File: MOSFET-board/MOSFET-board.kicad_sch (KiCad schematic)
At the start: 5 parts, among them J2 DB15_Female, J3 DB15_Female, J4 Bus_PCI_Express_x16, U11 PCF8575_Breakout

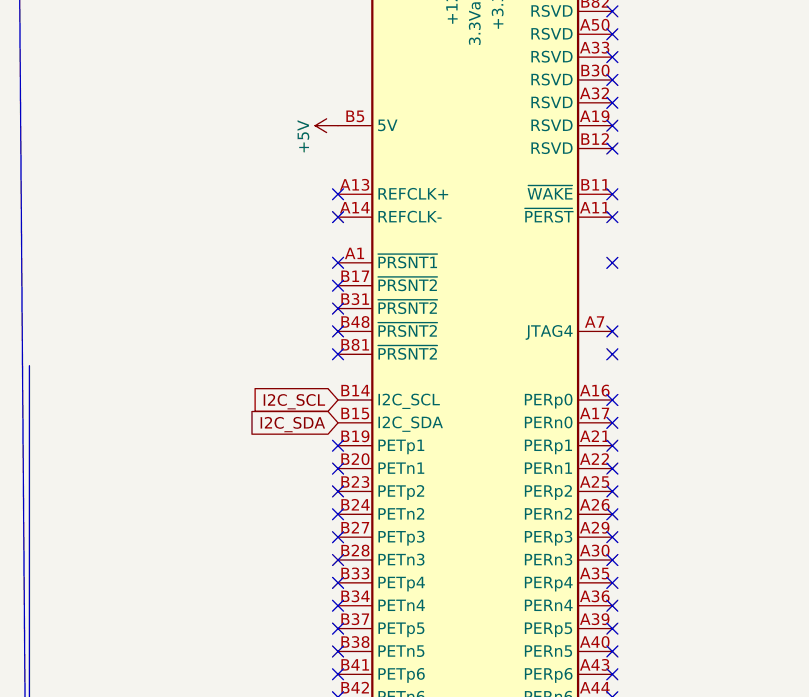
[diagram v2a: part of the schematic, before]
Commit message: mosfet board updates. GND tracing removals and aux scl/sda
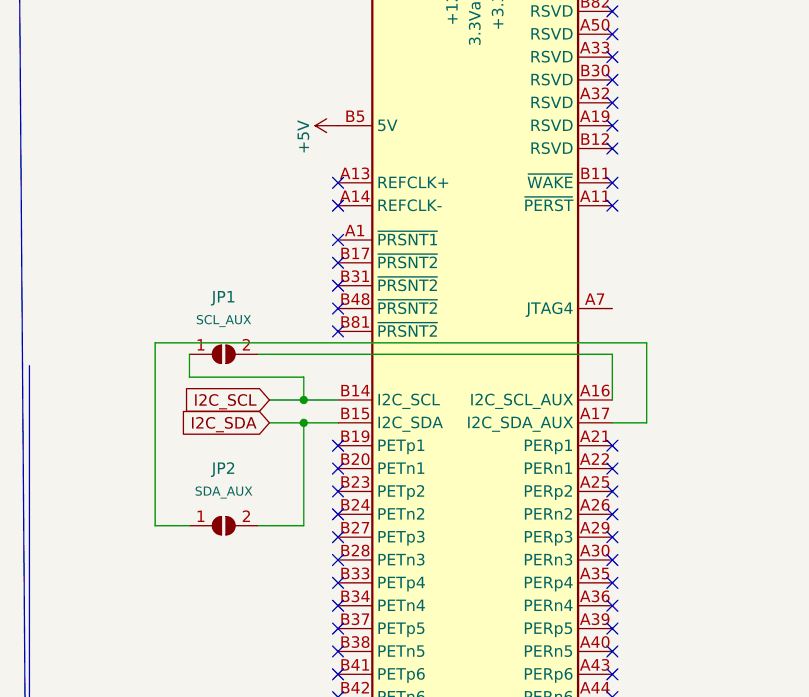
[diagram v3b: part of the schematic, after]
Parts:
- added JP1: SCL_AUX, Jumper:SolderJumper-2_P1.3mm_Open_Pad1.0x1.5mm, symbol Jumper:SolderJumper_2_Open
- added JP2: SDA_AUX, Jumper:SolderJumper-2_P1.3mm_Open_Pad1.0x1.5mm, symbol Jumper:SolderJumper_2_Open
- J4: footprint Connector_PCBEdge:BUS_PCIexpress_x16 -> PCIe_x16_DAQ:Custom-16x-PCIELock
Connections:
- net I2C_SCL: now also JP1.1 (A)
- net I2C_SDA: now also JP2.2 (B)
- net at J4.A16 (I2C_SCL_AUX): now also JP1.2 (B)
- net at J4.A17 (I2C_SDA_AUX): now also JP2.1 (A)
- no-connect marks 98 -> 93
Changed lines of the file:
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@@
   (junction (at 63.5 250.19) (diameter 0) (color 0 0 0 0)
   )
+  (junction (at 43.18 82.55) (diameter 0) (color 0 0 0 0)
+  )
   (junction (at 21.59 255.524) (diameter 0) (color 0 0 0 0)
   )
@@
   )
   (junction (at 21.59 250.444) (diameter 0) (color 0 0 0 0)
+  )
+  (junction (at 43.18 85.09) (diameter 0) (color 0 0 0 0)
   )
   (no_connect (at 77.47 115.57))
@@
   (no_connect (at 77.47 135.89))
   (no_connect (at 74.93 275.59))
-  (no_connect (at 46.99 62.23))
+  (no_connect (at 46.99 60.96))
   (no_connect (at 46.99 97.79))
   (no_connect (at 77.47 161.29))
@@
   (no_connect (at 77.47 113.03))
   (no_connect (at 29.21 208.28))
-  (no_connect (at 46.99 77.47))
+  (no_connect (at 46.99 64.77))
   (no_connect (at 46.99 95.25))
   (no_connect (at 77.47 105.41))
@@
   (no_connect (at 77.47 133.35))
   (no_connect (at 77.47 128.27))
-  (no_connect (at 77.47 62.23))
+  (no_connect (at 77.47 60.96))
   (no_connect (at 46.99 148.59))
-  (no_connect (at 77.47 85.09))
   (no_connect (at 46.99 113.03))
   (no_connect (at 77.47 146.05))
@@
   (no_connect (at 46.99 74.93))
   (no_connect (at 74.93 273.05))
-  (no_connect (at 77.47 82.55))
   (no_connect (at 33.02 273.304))
   (no_connect (at 57.15 205.74))
@@
   (no_connect (at 77.47 156.21))
   (no_connect (at 33.02 270.764))
-  (no_connect (at 77.47 67.31))
   (no_connect (at 33.02 268.224))
   (no_connect (at 46.99 151.13))
@@
   (no_connect (at 77.47 110.49))
   (no_connect (at 46.99 125.73))
-  (no_connect (at 77.47 74.93))
   (no_connect (at 77.47 44.45))
   (no_connect (at 57.15 208.28))
   (no_connect (at 77.47 95.25))
   (no_connect (at 77.47 123.19))
-  (no_connect (at 46.99 59.69))
-  (no_connect (at 77.47 77.47))
+  (no_connect (at 46.99 58.42))
   (no_connect (at 29.21 203.2))
   (no_connect (at 46.99 133.35))
@@
   (no_connect (at 77.47 125.73))
   (no_connect (at 77.47 49.53))
-  (no_connect (at 77.47 59.69))
+  (no_connect (at 77.47 58.42))
   (wire (pts (xy 33.02 245.364) (xy 21.59 245.364))
     (stroke (width 0) (type default))
@@
     (stroke (width 0) (type default))
   )
+  (wire (pts (xy 26.67 76.2) (xy 26.67 96.52))
+    (stroke (width 0) (type default))
+  )
   (wire (pts (xy 222.758 143.002) (xy 222.758 144.272))
     (stroke (width 0) (type default))
@@
     (stroke (width 0) (type default))
   )
+  (wire (pts (xy 77.47 85.09) (xy 81.28 85.09))
+    (stroke (width 0) (type default))
+  )
   (wire (pts (xy 62.23 30.48) (xy 64.77 30.48))
     (stroke (width 0) (type default))
   )
+  (wire (pts (xy 38.1 96.52) (xy 43.18 96.52))
+    (stroke (width 0) (type default))
+  )
+  (wire (pts (xy 81.28 85.09) (xy 81.28 76.2))
+    (stroke (width 0) (type default))
+  )
   (polyline (pts (xy 11.684 216.662) (xy 11.938 279.4))
     (stroke (width 0) (type default))
@@
     (stroke (width 0) (type default))
   )
+  (wire (pts (xy 43.18 96.52) (xy 43.18 85.09))
+    (stroke (width 0) (type default))
+  )
   (wire (pts (xy 63.5 255.27) (xy 74.93 255.27))
     (stroke (width 0) (type default))
@@
     (stroke (width 0) (type default))
   )
+  (wire (pts (xy 26.67 96.52) (xy 30.48 96.52))
+    (stroke (width 0) (type default))
+  )
   (wire (pts (xy 21.59 260.604) (xy 21.59 265.684))
     (stroke (width 0) (type default))
@@
     (stroke (width 0) (type default))
   )
+  (wire (pts (xy 43.18 82.55) (xy 46.99 82.55))
+    (stroke (width 0) (type default))
+  )
   (wire (pts (xy 203.454 144.272) (xy 203.454 143.002))
     (stroke (width 0) (type default))
@@
     (stroke (width 0) (type default))
   )
+  (wire (pts (xy 81.28 76.2) (xy 26.67 76.2))
+    (stroke (width 0) (type default))
+  )
   (wire (pts (xy 52.07 20.32) (xy 54.61 20.32))
     (stroke (width 0) (type default))
@@
     (stroke (width 0) (type default))
   )
+  (wire (pts (xy 43.18 85.09) (xy 46.99 85.09))
+    (stroke (width 0) (type default))
+  )
   (wire (pts (xy 64.77 29.21) (xy 64.77 30.48))
     (stroke (width 0) (type default))
@@
     (stroke (width 0) (type default))
   )
+  (wire (pts (xy 39.37 82.55) (xy 43.18 82.55))
+    (stroke (width 0) (type default))
+  )
   (polyline (pts (xy 118.11 154.94) (xy 233.68 154.94))
     (stroke (width 0) (type default))
@@
     (stroke (width 0) (type default))
   )
+  (wire (pts (xy 30.48 77.47) (xy 30.48 80.01))
+    (stroke (width 0) (type default))
+  )
   (polyline (pts (xy 12.7 12.7) (xy 233.68 12.7))
     (stroke (width 0) (type default))
@@
     (stroke (width 0) (type default))
   )
+  (wire (pts (xy 77.47 77.47) (xy 38.1 77.47))
+    (stroke (width 0) (type default))
+  )
+  (wire (pts (xy 30.48 80.01) (xy 43.18 80.01))
+    (stroke (width 0) (type default))
+  )
   (polyline (pts (xy 118.11 147.32) (xy 142.24 147.32))
     (stroke (width 0) (type default))
@@
     (stroke (width 0) (type default))
   )
+  (wire (pts (xy 77.47 82.55) (xy 77.47 77.47))
+    (stroke (width 0) (type default))
+  )
   (wire (pts (xy 62.23 30.48) (xy 62.23 31.75))
     (stroke (width 0) (type default))
@@
     (stroke (width 0) (type default))
   )
+  (wire (pts (xy 43.18 80.01) (xy 43.18 82.55))
+    (stroke (width 0) (type default))
+  )
   (wire (pts (xy 40.64 222.25) (xy 40.64 229.87))
+    (stroke (width 0) (type default))
+  )
+  (wire (pts (xy 39.37 85.09) (xy 43.18 85.09))
     (stroke (width 0) (type default))
   )
@@
     )
   )
-  (global_label "I2C_SDA" (shape input) (at 46.99 85.09 180) (fields_autoplaced)
-    (effects (font (size 1.27 1.27)) (justify right))
-    (property "Intersheetrefs" "${INTERSHEET_REFS}" (at 36.9569 85.0106 0)
+  (global_label "I2C_SDA" (shape input) (at 39.37 85.09 180) (fields_autoplaced)
+    (effects (font (size 1.27 1.27)) (justify right))
+    (property "Intersheetrefs" "${INTERSHEET_REFS}" (at 29.3369 85.0106 0)
       (effects (font (size 1.27 1.27)) (justify right) hide)
     )
@@
     )
   )
-  (global_label "I2C_SCL" (shape input) (at 46.99 82.55 180) (fields_autoplaced)
-    (effects (font (size 1.27 1.27)) (justify right))
-    (property "Intersheetrefs" "${INTERSHEET_REFS}" (at 36.4453 82.55 0)
+  (global_label "I2C_SCL" (shape input) (at 39.37 82.55 180) (fields_autoplaced)
+    (effects (font (size 1.27 1.27)) (justify right))
+    (property "Intersheetrefs" "${INTERSHEET_REFS}" (at 28.8253 82.55 0)
       (effects (font (size 1.27 1.27)) (justify right) hide)
     )
@@
     )
   )
+  (symbol (lib_id "Jumper:SolderJumper_2_Open") (at 34.29 96.52 0) (unit 1)
+    (in_bom yes) (on_board yes) (dnp no) (fields_autoplaced)
+    (property "Reference" "JP2" (at 34.29 90.17 0)
+      (effects (font (size 1.27 1.27)))
+    )
+    (property "Value" "SDA_AUX" (at 34.29 92.71 0)
+      (effects (font (size 1 1)))
+    )
+    (property "Footprint" "Jumper:SolderJumper-2_P1.3mm_Open_Pad1.0x1.5mm" (at 34.29 96.52 0)
+      (effects (font (size 1.27 1.27)) hide)
+    )
+    (property "Datasheet" "~" (at 34.29 96.52 0)
+      (effects (font (size 1.27 1.27)) hide)
+    )
+    (pin "1")
+    (pin "2")
+    (instances
+      (project "MOSFET-board"
+        (path "/eeff6235-4c56-4b47-a90f-883101560994"
+          (reference "JP2") (unit 1)
+        )
+      )
+    )
+  )
   (symbol (lib_id "power:+3.3V") (at 203.454 143.002 0) (unit 1)
     (in_bom yes) (on_board yes) (dnp no)
@@
       (effects (font (size 1.27 1.27)) (justify left))
     )
-    (property "Footprint" "Connector_PCBEdge:BUS_PCIexpress_x16" (at 58.42 80.01 0)
+    (property "Footprint" "PCIe_x16_DAQ:Custom-16x-PCIELock" (at 58.42 80.01 0)
       (effects (font (size 1.27 1.27)) hide)
     )
@@
         )
       )
+    )
+  )
+  (symbol (lib_id "Jumper:SolderJumper_2_Open") (at 34.29 77.47 0) (unit 1)
+    (in_bom yes) (on_board yes) (dnp no) (fields_autoplaced)
+    (property "Reference" "JP1" (at 34.29 71.12 0)
+      (effects (font (size 1.27 1.27)))
+    )
+    (property "Value" "SCL_AUX" (at 34.29 73.66 0)
+      (effects (font (size 1 1)))
+    )
+    (property "Footprint" "Jumper:SolderJumper-2_P1.3mm_Open_Pad1.0x1.5mm" (at 34.29 77.47 0)
+      (effects (font (size 1.27 1.27)) hide)
+    )
+    (property "Datasheet" "~" (at 34.29 77.47 0)
+      (effects (font (size 1.27 1.27)) hide)
+    )
+    (pin "1")
+    (pin "2")
+    (instances
+      (project "MOSFET-board"
+        (path "/eeff6235-4c56-4b47-a90f-883101560994"
+          (reference "JP1") (unit 1)
+        )
+      )
